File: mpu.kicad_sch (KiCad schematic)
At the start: 14 parts, among them IC19 MC6809E, SW1 RESET

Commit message: validate component values
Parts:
- C22: DigiKey (none) -> 732-8598-1-ND
- C23: DigiKey (none) -> 732-8762-1-ND
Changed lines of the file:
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@@
       (effects (font (size 1.27 1.27)) hide)
     )
-    (property "Datasheet" "~" (id 3) (at 173.863 58.674 0)
+    (property "Datasheet" "https://www.we-online.com/katalog/datasheet/860010372006.pdf" (id 3) (at 173.863 58.674 0)
+      (effects (font (size 1.27 1.27)) hide)
+    )
+    (property "DigiKey" "732-8598-1-ND" (id 4) (at 173.863 58.674 90)
       (effects (font (size 1.27 1.27)) hide)
     )
@@
       (effects (font (size 1.27 1.27)) hide)
     )
-    (property "Datasheet" "~" (id 3) (at 123.19 92.964 0)
-      (effects (font (size 1.27 1.27)) hide)
-    )
+    (property "Datasheet" "https://www.we-online.com/katalog/datasheet/860010772005.pdf" (id 3) (at 123.19 92.964 0)
+      (effects (font (size 1.27 1.27)) hide)
+    )
+    (property "DigiKey" "732-8762-1-ND" (id 4) (at 123.19 92.964 0)
+      (effects (font (size 1.27 1.27)) hide)
+    )

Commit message: update part numbers
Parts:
- C23: DigiKey 732-8762-1-ND -> 732-8966-1-ND
- C4: footprint Capacitor_THT:C_Disc_D3.0mm_W2.0mm_P2.50mm -> Capacitor_THT:C_Disc_D4.3mm_W1.9mm_P5.00mm; DigiKey (none) -> BC1101CT-ND
- D4, D5, D6: DigiKey (none) -> 1N914FS-ND
- IC19: Note (none) -> donor
- SW1: DigiKey (none) -> 401-1225-ND
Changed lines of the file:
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@@
+      (effects (font (size 1.27 1.27)) hide)
+    )
+    (property "DigiKey" "1N914FS-ND" (id 4) (at 90.678 91.694 0)
       (effects (font (size 1.27 1.27)) hide)
     )
@@
       (effects (font (size 1.27 1.27)) hide)
     )
+    (property "DigiKey" "1N914FS-ND" (id 4) (at 80.518 91.694 0)
+      (effects (font (size 1.27 1.27)) hide)
+    )
     (pin "1")
     (pin "2")
@@
       (effects (font (size 1.27 1.27)) hide)
     )
+    (property "DigiKey" "1N914FS-ND" (id 4) (at 80.518 101.854 0)
+      (effects (font (size 1.27 1.27)) hide)
+    )
     (pin "1")
     (pin "2")
@@
       (effects (font (size 1.27 1.27)) hide)
     )
-    (property "Datasheet" "~" (id 3) (at 114.808 103.124 0)
+    (property "Datasheet" "https://www.ckswitches.com/media/1402/fpush.pdf" (id 3) (at 114.808 103.124 0)
+      (effects (font (size 1.27 1.27)) hide)
+    )
+    (property "DigiKey" "401-1225-ND" (id 4) (at 109.728 103.124 90)
       (effects (font (size 1.27 1.27)) hide)
     )
@@
       (effects (font (size 1.27 1.27)) (justify left))
     )
-    (property "Footprint" "Capacitor_THT:C_Disc_D3.0mm_W2.0mm_P2.50mm" (id 2) (at 90.678 101.854 0)
-      (effects (font (size 1.27 1.27)) hide)
-    )
-    (property "Datasheet" "~" (id 3) (at 90.678 101.854 0)
+    (property "Footprint" "Capacitor_THT:C_Disc_D4.3mm_W1.9mm_P5.00mm" (id 2) (at 90.678 101.854 0)
+      (effects (font (size 1.27 1.27)) hide)
+    )
+    (property "Datasheet" "https://www.vishay.com/docs/45171/kseries.pdf" (id 3) (at 90.678 101.854 0)
+      (effects (font (size 1.27 1.27)) hide)
+    )
+    (property "DigiKey" "BC1101CT-ND" (id 4) (at 90.678 101.854 0)
       (effects (font (size 1.27 1.27)) hide)
     )
@@
       (effects (font (size 1.27 1.27)) hide)
     )
-    (property "Datasheet" "https://www.we-online.com/katalog/datasheet/860010772005.pdf" (id 3) (at 123.19 92.964 0)
-      (effects (font (size 1.27 1.27)) hide)
-    )
-    (property "DigiKey" "732-8762-1-ND" (id 4) (at 123.19 92.964 0)
+    (property "Datasheet" "https://www.we-online.com/katalog/datasheet/860020772005.pdf" (id 3) (at 123.19 92.964 0)
+      (effects (font (size 1.27 1.27)) hide)
+    )
+    (property "DigiKey" "732-8966-1-ND" (id 4) (at 123.19 92.964 0)
       (effects (font (size 1.27 1.27)) hide)
     )
@@
       (effects (font (size 1.27 1.27)) hide)
     )
+    (property "Note" "donor" (id 4) (at 168.148 94.234 0)
+      (effects (font (size 1.27 1.27)) hide)
+    )

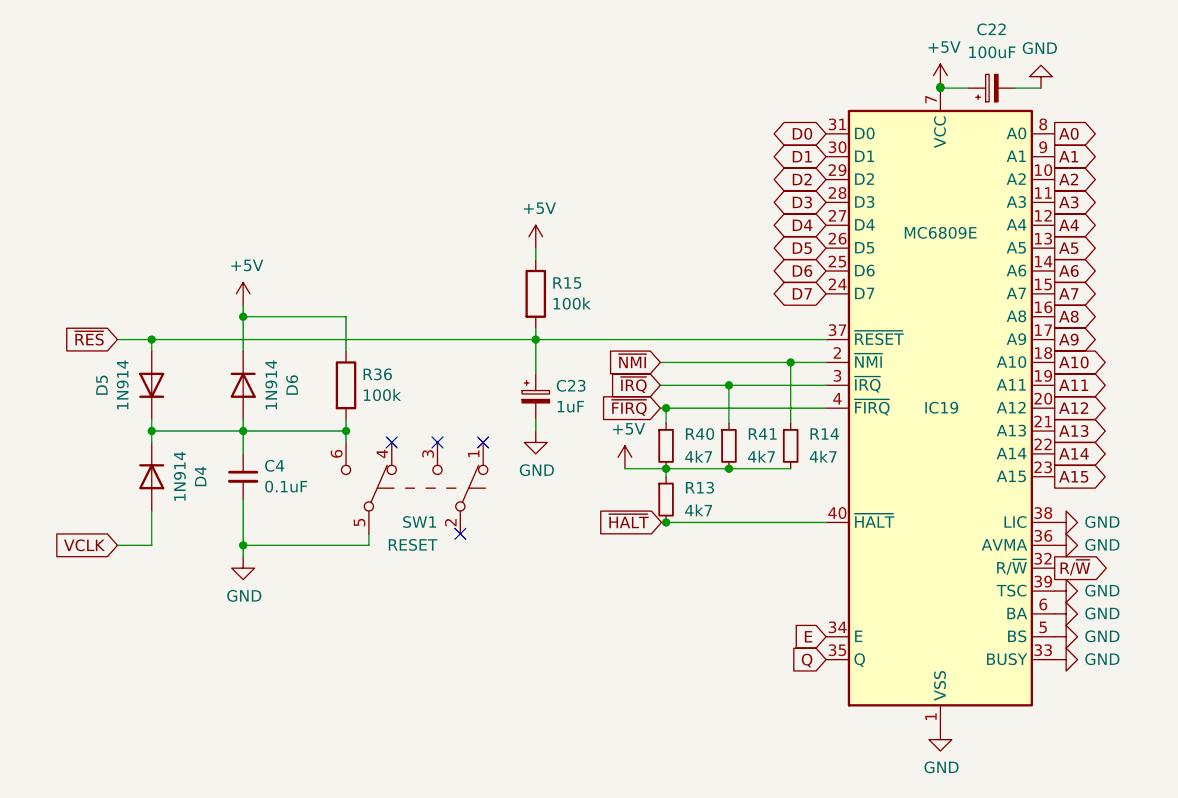
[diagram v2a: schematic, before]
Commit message: resolve part numbers
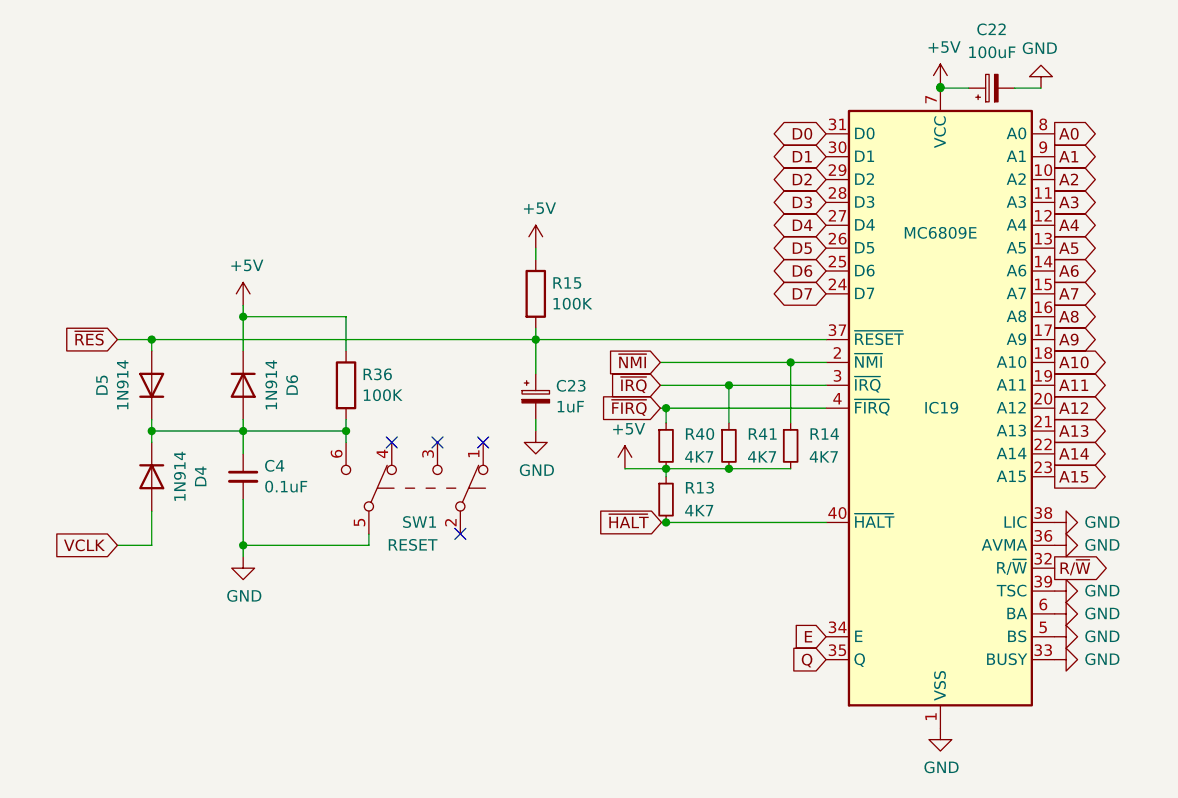
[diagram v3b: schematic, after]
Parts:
- R13, R14, R40, R41: value 4k7 -> 4K7; DigiKey (none) -> CF14JT4K70CT-ND
- R15, R36: value 100k -> 100K; DigiKey (none) -> CF14JT100KCT-ND
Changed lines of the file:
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@@
       (effects (font (size 1.27 1.27)) (justify left))
     )
-    (property "Value" "4k7" (id 1) (at 139.7 105.6639 0)
+    (property "Value" "4K7" (id 1) (at 139.7 105.6639 0)
       (effects (font (size 1.27 1.27)) (justify left))
     )
@@
     )
     (property "Datasheet" "~" (id 3) (at 137.668 104.394 0)
+      (effects (font (size 1.27 1.27)) hide)
+    )
+    (property "DigiKey" "CF14JT4K70CT-ND" (id 4) (at 137.668 104.394 0)
       (effects (font (size 1.27 1.27)) hide)
     )
@@
       (effects (font (size 1.27 1.27)) (justify left))
     )
-    (property "Value" "100k" (id 1) (at 124.968 82.677 0)
+    (property "Value" "100K" (id 1) (at 124.968 82.677 0)
       (effects (font (size 1.27 1.27)) (justify left))
     )
@@
     )
     (property "Datasheet" "~" (id 3) (at 123.19 81.534 0)
+      (effects (font (size 1.27 1.27)) hide)
+    )
+    (property "DigiKey" "CF14JT100KCT-ND" (id 4) (at 123.19 81.534 0)
       (effects (font (size 1.27 1.27)) hide)
     )
@@
       (effects (font (size 1.27 1.27)) (justify left))
     )
-    (property "Value" "100k" (id 1) (at 103.886 92.837 0)
+    (property "Value" "100K" (id 1) (at 103.886 92.837 0)
       (effects (font (size 1.27 1.27)) (justify left))
     )
@@
     )
     (property "Datasheet" "~" (id 3) (at 102.108 91.694 0)
+      (effects (font (size 1.27 1.27)) hide)
+    )
+    (property "DigiKey" "CF14JT100KCT-ND" (id 4) (at 102.108 91.694 0)
       (effects (font (size 1.27 1.27)) hide)
     )
@@
       (effects (font (size 1.27 1.27)) (justify left))
     )
-    (property "Value" "4k7" (id 1) (at 146.685 99.6949 0)
+    (property "Value" "4K7" (id 1) (at 146.685 99.6949 0)
       (effects (font (size 1.27 1.27)) (justify left))
     )
@@
       (effects (font (size 1.27 1.27)) hide)
     )
+    (property "DigiKey" "CF14JT4K70CT-ND" (id 4) (at 144.653 98.425 0)
+      (effects (font (size 1.27 1.27)) hide)
+    )
     (pin "1")
     (pin "2")
@@
       (effects (font (size 1.27 1.27)) (justify left))
     )
-    (property "Value" "4k7" (id 1) (at 153.543 99.6949 0)
+    (property "Value" "4K7" (id 1) (at 153.543 99.6949 0)
       (effects (font (size 1.27 1.27)) (justify left))
     )
@@
       (effects (font (size 1.27 1.27)) hide)
     )
+    (property "DigiKey" "CF14JT4K70CT-ND" (id 4) (at 151.511 98.425 0)
+      (effects (font (size 1.27 1.27)) hide)
+    )
     (pin "1")
     (pin "2")
@@
       (effects (font (size 1.27 1.27)) (justify left))
     )
-    (property "Value" "4k7" (id 1) (at 139.7 99.6949 0)
+    (property "Value" "4K7" (id 1) (at 139.7 99.6949 0)
       (effects (font (size 1.27 1.27)) (justify left))
     )
@@
       (effects (font (size 1.27 1.27)) hide)
     )
+    (property "DigiKey" "CF14JT4K70CT-ND" (id 4) (at 137.668 98.425 0)
+      (effects (font (size 1.27 1.27)) hide)
+    )
